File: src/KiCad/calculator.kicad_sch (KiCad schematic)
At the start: 48 parts, among them J1 USB_C_Receptacle_USB2.0_14P, SW1 1, SW10 0, SW11 ., SW12 x10, SW13 DEL, SW14 x, SW15 +, SW16 Ans, SW17 AC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

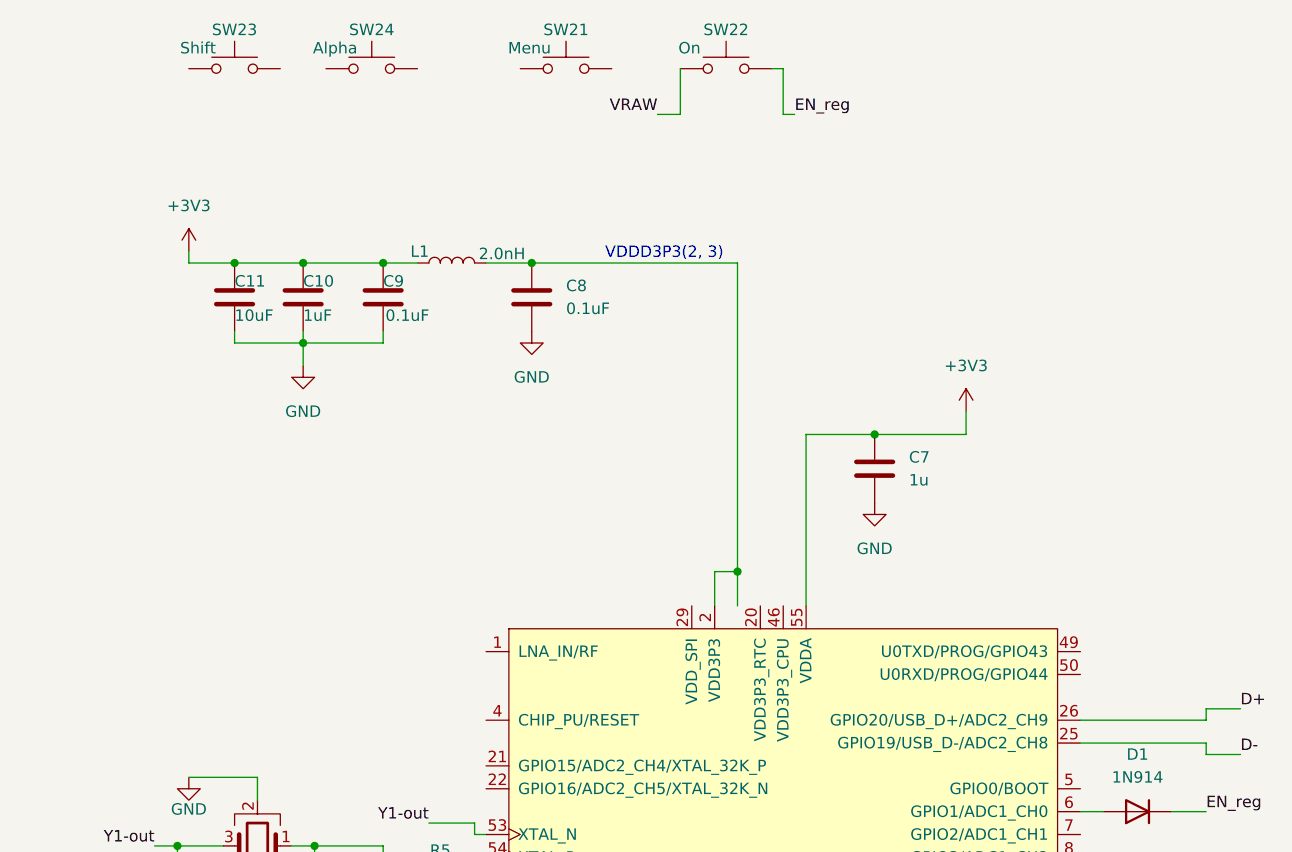
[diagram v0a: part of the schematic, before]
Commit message: Chip is powered
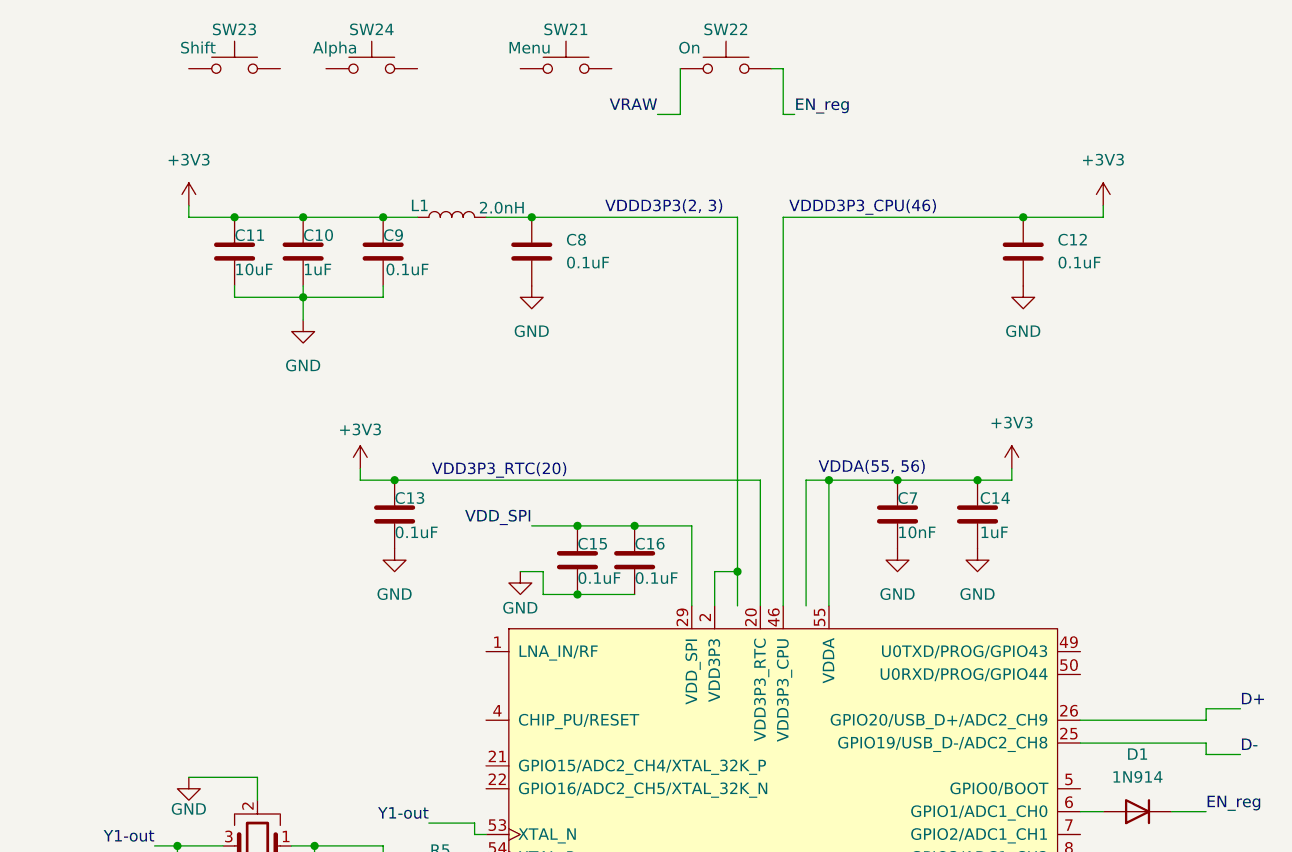
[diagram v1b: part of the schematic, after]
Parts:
- added C12, C13, C15, C16: 0.1uF, symbol Device:C
- added C14: 1uF, symbol Device:C
- C7: value 1u -> 10nF
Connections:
- net +3V3: now also U4.20 (VDD3P3_RTC), U4.46 (VDD3P3_CPU), C12.1, C13.1, C14.1
- net GND: now also C12.2, C13.2, C14.2, C15.2, C16.2
- net VDD_SPI: now reaches U4.29 (VDD_SPI)
- net VDD_SPI: now also C15.1, C16.1
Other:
- note added: "VDD3P3_RTC(20)"
- note added: "VDDA(55, 56)"
- note added: "VDDD3P3_CPU(46)"
- moved on the sheet: C10, C11, C7, C8, C9, L1

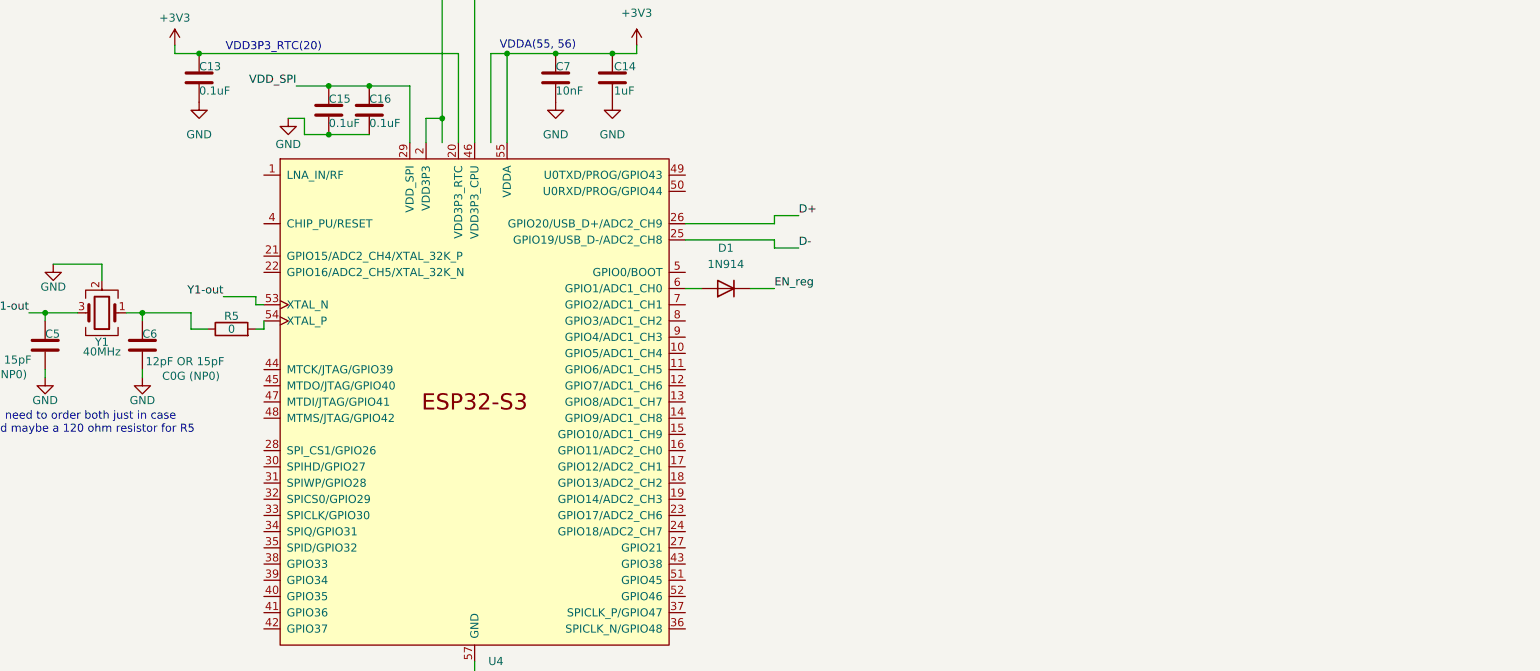
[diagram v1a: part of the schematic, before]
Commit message: flash wired
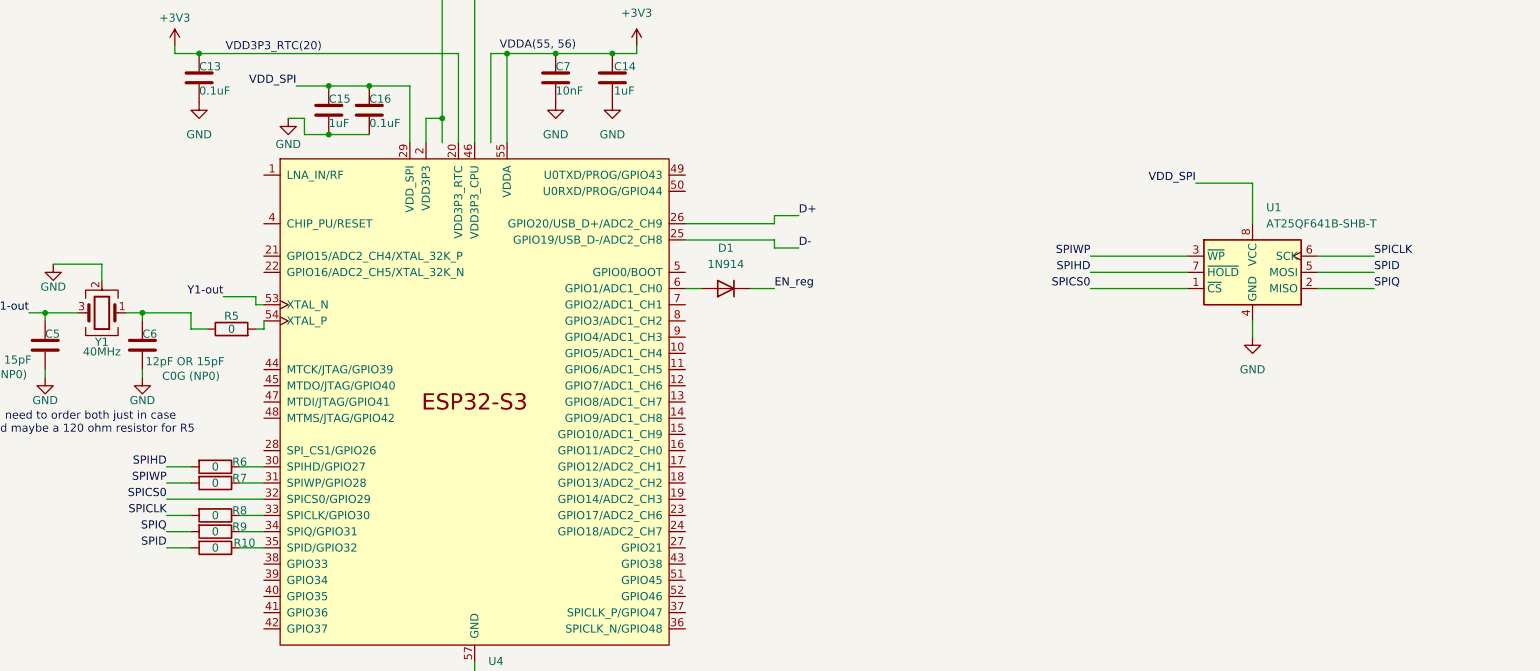
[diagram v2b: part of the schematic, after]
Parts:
- added R10, R6, R7, R8, R9: 0, symbol Device:R
- added U1: AT25QF641B-SHB-T, symbol Memory_EEPROM:AT25xxx
- C15: value 0.1uF -> 1uF
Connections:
- net GND: now also U1.4 (GND)
- net VDD_SPI: now also U1.8 (VCC)
- net at U4.30 (SPIHD/GPIO27): now also R6.1
- net at U4.31 (SPIWP/GPIO28): now also R7.1
- net SPICS0: now reaches U4.32 (SPICS0/GPIO29)
- net SPICS0: now also U1.1 (~{CS})
- net at U4.33 (SPICLK/GPIO30): now also R8.1
- net at U4.34 (SPIQ/GPIO31): now also R9.1
- net at U4.35 (SPID/GPIO32): now also R10.1
- new net SPICLK: R8.2, U1.6 (SCK)
- new net SPID: R10.2, U1.5 (MOSI)
- new net SPIHD: R6.2, U1.7 (~{HOLD})
- new net SPIQ: R9.2, U1.2 (MISO)
- new net SPIWP: R7.2, U1.3 (~{WP})

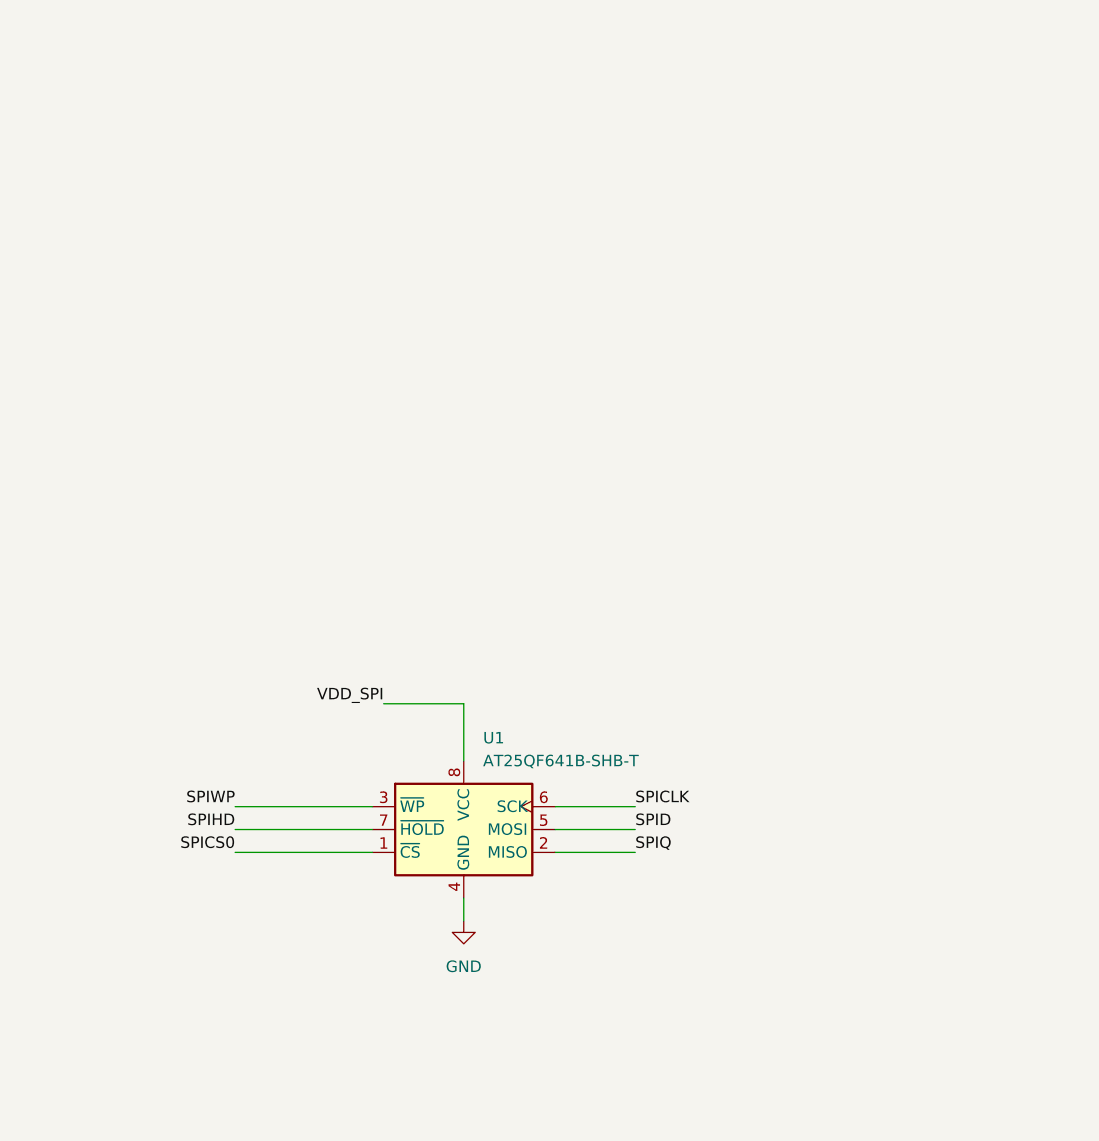
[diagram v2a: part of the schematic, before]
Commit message: Updated flash memory sector
To make writing safer added a 1uF cap
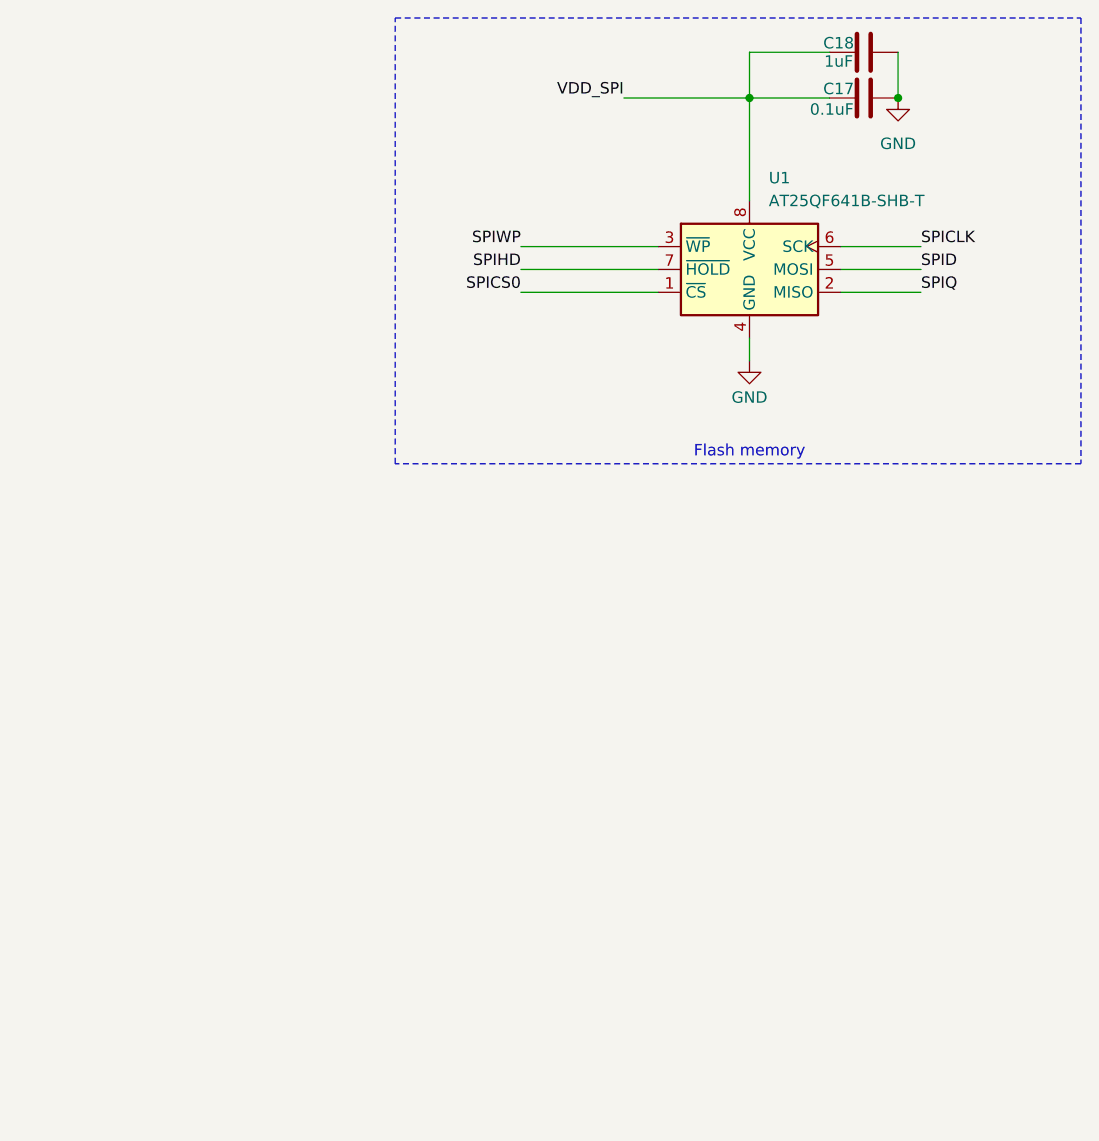
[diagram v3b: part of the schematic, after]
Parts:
- added C17: 0.1uF, symbol Device:C
- added C18: 1uF, symbol Device:C
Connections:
- net GND: now also C17.2, C18.2
- net VDD_SPI: now also C17.1, C18.1
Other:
- note added: "Flash memory"
- moved on the sheet: U1

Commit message: CHIP_PU
also made the PCB 4 layers
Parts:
- added C19: 1uF, symbol Device:C
- added R11: 10k, symbol Device:R
- added SW25, SW27, SW29: Shift, symbol Switch:SW_Push
- added SW26, SW28, SW30: Alpha, symbol Switch:SW_Push
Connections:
- net +3V3: now also R11.1
- net GND: now also C19.2
- net at U4.4 (CHIP_PU/RESET): now also C19.1, R11.2
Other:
- moved on the sheet: SW21, SW22, SW23, SW24

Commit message: Antenna
I added the antenna and its pi cell which will be used if needed.
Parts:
- added AE1: 2450AT18E0100E, symbol Device:Antenna_Shield
- added C20, C21: DNP, symbol Device:C
- added L2: 0R, symbol Device:L
- added SW31: Up, symbol Switch:SW_Push
- added SW32: L, symbol Switch:SW_Push
- added SW33: R, symbol Switch:SW_Push
- added SW34: Down, symbol Switch:SW_Push
- added SW35, SW37, SW39, SW41, SW43, SW45, SW47, SW51: Shift, symbol Switch:SW_Push
- added SW36, SW38, SW40, SW42, SW44, SW46, SW48, SW52: Alpha, symbol Switch:SW_Push
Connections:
- net GND: now also AE1.2 (Shield), C20.2, C21.2
- net F_row0: now reaches SW25.1
- net F_row0: now also SW26.1, SW27.1, SW28.1, SW29.1, SW30.1
- net F_col0: now reaches SW25.2
- net F_col0: now also SW23.2, SW35.2, SW41.2, SW47.2
- net F_col3: now reaches SW28.2
- net F_col3: now also SW38.2, SW44.2
- net F_col5: now reaches SW30.2
- net F_col5: now also SW40.2, SW46.2, SW52.2
- net F_col4: now reaches SW29.2
- net F_col4: now also SW21.2, SW39.2, SW45.2, SW51.2
- net at SW26.2: now also SW36.2, SW42.2, SW48.2
- net F_row4: now reaches SW21.1
- net F_row4: now also SW23.1, SW24.1
- net F_col1: now reaches SW24.2
- net LNA_IN: now reaches U4.1 (LNA_IN/RF)
- net LNA_IN: now also C20.1, L2.1
- net F_col2: now reaches SW27.2
- net F_col2: now also SW37.2, SW43.2
- new net: AE1.1 (A), C21.1, L2.2
- new net F_row1: SW35.1, SW36.1, SW37.1, SW38.1, SW39.1, SW40.1
- new net F_row2: SW41.1, SW42.1, SW43.1, SW44.1, SW45.1, SW46.1
- new net F_row3: SW47.1, SW48.1, SW51.1, SW52.1
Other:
- note added: "* Will support WI-FI and Bluetooth"
- note added: "-Will use mechanical switches"
- note added: "2.4Ghz Pi-cell + antenna chip"
- moved on the sheet: SW21, SW22, SW25, SW26, SW27, SW28, SW29, SW30

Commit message: Fixes to data lines + main grid
I added Resistors to the D+/- lines and connected the main key grid to the s3.
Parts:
- added C22: DNP, symbol Device:C
- added C23: C, symbol Device:C
- added R12, R13: 33, symbol Device:R
- SW17: value AC -> AC/OFF
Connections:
- net Col 0: now also U4.7 (GPIO2/ADC1_CH1)
- net Col 1: now also U4.8 (GPIO3/ADC1_CH2)
- net Col 2: now also U4.9 (GPIO4/ADC1_CH3)
- net Col 3: now also U4.10 (GPIO5/ADC1_CH4)
- net Col 4: now also U4.11 (GPIO6/ADC1_CH5)
- net D+: now also C22.2, R12.2; no longer U4.26 (GPIO20/USB_D+/ADC2_CH9)
- net D-: now also C23.1, R13.2; no longer U4.25 (GPIO19/USB_D-/ADC2_CH8)
- net GND: now also C22.1, C23.2
- net Row 0: now also U4.15 (GPIO10/ADC1_CH9)
- net Row 1: now also U4.14 (GPIO9/ADC1_CH8)
- net Row 2: now also U4.13 (GPIO8/ADC1_CH7)
- net Row 3: now also U4.12 (GPIO7/ADC1_CH6)
- new net: R12.1, U4.26 (GPIO20/USB_D+/ADC2_CH9)
- new net: R13.1, U4.25 (GPIO19/USB_D-/ADC2_CH8)
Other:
- note added: "also this needs to be as close to the chip"
- note added: "maybe just add the footprints to the PCB?"
- note added: "might add anti-ghosting"

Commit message: Fixes and function grid
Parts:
- added D2, D3, D4: D_TVS, symbol Device:D_TVS
- added R14: 10k, symbol Device:R
- added TP1: Firmware, symbol Connector:TestPoint
- added TP2: GND, symbol Connector:TestPoint
- added TP3: RESET, symbol Connector:TestPoint
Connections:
- net +3V3: now also R14.2
- net D+: now also D3.1 (A1)
- net D-: now also D2.2 (A2)
- net F_col0: now also U4.24 (GPIO18/ADC2_CH7)
- net F_col1: now also SW26.2, SW36.2, SW42.2, SW48.2, U4.27 (GPIO21)
- net F_col2: now also U4.43 (GPIO38)
- net F_col3: now also SW33.2, SW34.2, U4.37 (SPICLK_P/GPIO47)
- net F_col4: now also U4.36 (SPICLK_N/GPIO48)
- net F_col5: now also U4.42 (GPIO37)
- net F_row0: now also U4.23 (GPIO17/ADC2_CH6)
- net F_row1: now also U4.19 (GPIO14/ADC2_CH3)
- net F_row2: now also U4.18 (GPIO13/ADC2_CH2)
- net F_row3: now also SW32.1, SW34.1, U4.17 (GPIO12/ADC2_CH1)
- net F_row4: now also SW31.1, SW33.1, U4.16 (GPIO11/ADC2_CH0)
- net GND: now also D2.1 (A1), D3.2 (A2), D4.1 (A1), TP2.1
- net VCC: now also D4.2 (A2)
- net at C19.1, R11.2, U4.4 (CHIP_PU/RESET): now also TP3.1
- net at U4.5 (GPIO0/BOOT): now also R14.1, TP1.1
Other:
- note added: "Low capacitance!"
- note added: "can be up to 47k"
- moved on the sheet: C22, C23, R12, R13, SW21, SW23, SW24, SW31, SW32, SW33, SW34

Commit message: screen is connected, and i added a io expander
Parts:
- added C24: 100nF, symbol Device:C
- added J2: screen fpc, symbol Connector:Conn_01x16_Socket
- added R15: 10k, symbol Device:R
- added U5: MCP23S17x-x-ML, Package_DFN_QFN:QFN-28-1EP_6x6mm_P0.65mm_EP4.25x4.25mm, symbol Interface_Expansion:MCP23S17x-x-ML
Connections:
- net +3V3: now also C24.1, J2.15 (Pin_15), R15.1, U5.5 (V_{DD})
- net F_col0: now also U5.22 (GPA5); no longer U4.24 (GPIO18/ADC2_CH7)
- net F_col1: now also U5.23 (GPA6); no longer U4.27 (GPIO21)
- net F_col2: now also U5.24 (GPA7); no longer U4.43 (GPIO38)
- net F_col3: now also U5.25 (GPB0); no longer U4.37 (SPICLK_P/GPIO47)
- net F_col4: now also U5.26 (GPB1); no longer U4.36 (SPICLK_N/GPIO48)
- net F_col5: now also U5.27 (GPB2); no longer U4.42 (GPIO37)
- net F_row0: now also U5.21 (GPA4); no longer U4.23 (GPIO17/ADC2_CH6)
- net F_row1: now also U5.20 (GPA3); no longer U4.19 (GPIO14/ADC2_CH3)
- net F_row2: now also U5.19 (GPA2); no longer U4.18 (GPIO13/ADC2_CH2)
- net F_row3: now also U5.18 (GPA1); no longer U4.17 (GPIO12/ADC2_CH1)
- net F_row4: now also U5.17 (GPA0); no longer U4.16 (GPIO11/ADC2_CH0)
- net GND: now also C24.2, J2.16 (Pin_16), U5.11 (A0), U5.12 (A1), U5.13 (A2), U5.29 (EP), U5.6 (V_{SS})
- net TFT_CS: now also U4.50 (U0RXD/PROG/GPIO44), J2.14 (Pin_14)
- net TFT_DC: now also U4.49 (U0TXD/PROG/GPIO43), J2.13 (Pin_13)
- net TFT_RST: now also U4.27 (GPIO21), J2.10 (Pin_10)
- net TFT_DB0: now reaches U4.38 (GPIO33)
- net TFT_DB0: now also J2.9 (Pin_9)
- net TFT_DB1: now reaches U4.39 (GPIO34)
- net TFT_DB1: now also J2.8 (Pin_8)
- net TFT_DB2: now reaches U4.40 (GPIO35)
- net TFT_DB2: now also J2.7 (Pin_7)
- net TFT_DB3: now reaches U4.41 (GPIO36)
- net TFT_DB3: now also J2.6 (Pin_6)
- net GPIO39: now reaches U4.44 (MTCK/JTAG/GPIO39)
- net GPIO39: now also J2.4 (Pin_4)
- net GPIO40: now reaches U4.45 (MTDO/JTAG/GPIO40)
- net GPIO40: now also J2.3 (Pin_3)
- net GPIO41: now reaches U4.47 (MTDI/JTAG/GPIO41)
- net GPIO41: now also J2.2 (Pin_2)
- net GPIO42: now reaches U4.48 (MTMS/JTAG/GPIO42)
- net GPIO42: now also J2.12 (Pin_12)
- new net: R15.2, U5.14 (~{RESET})
- new net IO_Ex-CS: U4.23 (GPIO17/ADC2_CH6), U5.7 (~{CS})
- new net IO_Ex-INTA: U4.16 (GPIO11/ADC2_CH0), U5.16 (INTA)
- new net IO_Ex-SCK: U4.19 (GPIO14/ADC2_CH3), U5.8 (SCK)
- new net IO_Ex-SI: U4.18 (GPIO13/ADC2_CH2), U5.9 (SI)
- new net IO_Ex-SO: U4.17 (GPIO12/ADC2_CH1), U5.10 (SO)
- new net TFT_BL: J2.1 (Pin_1), U4.43 (GPIO38)
- new net TFT_DB4: J2.5 (Pin_5), U4.42 (GPIO37)
- new net TFT_RD: J2.11 (Pin_11), U4.24 (GPIO18/ADC2_CH7)
- no-connect marks 0 -> 1
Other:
- note added: "45/46 are strapping"
- note added: "Adress = 0"
